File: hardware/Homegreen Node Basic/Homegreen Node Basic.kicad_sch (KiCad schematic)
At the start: 10 parts, among them J3 Conn_01x06_Pin, SW1 SW_Push, U1 ATtiny88-A

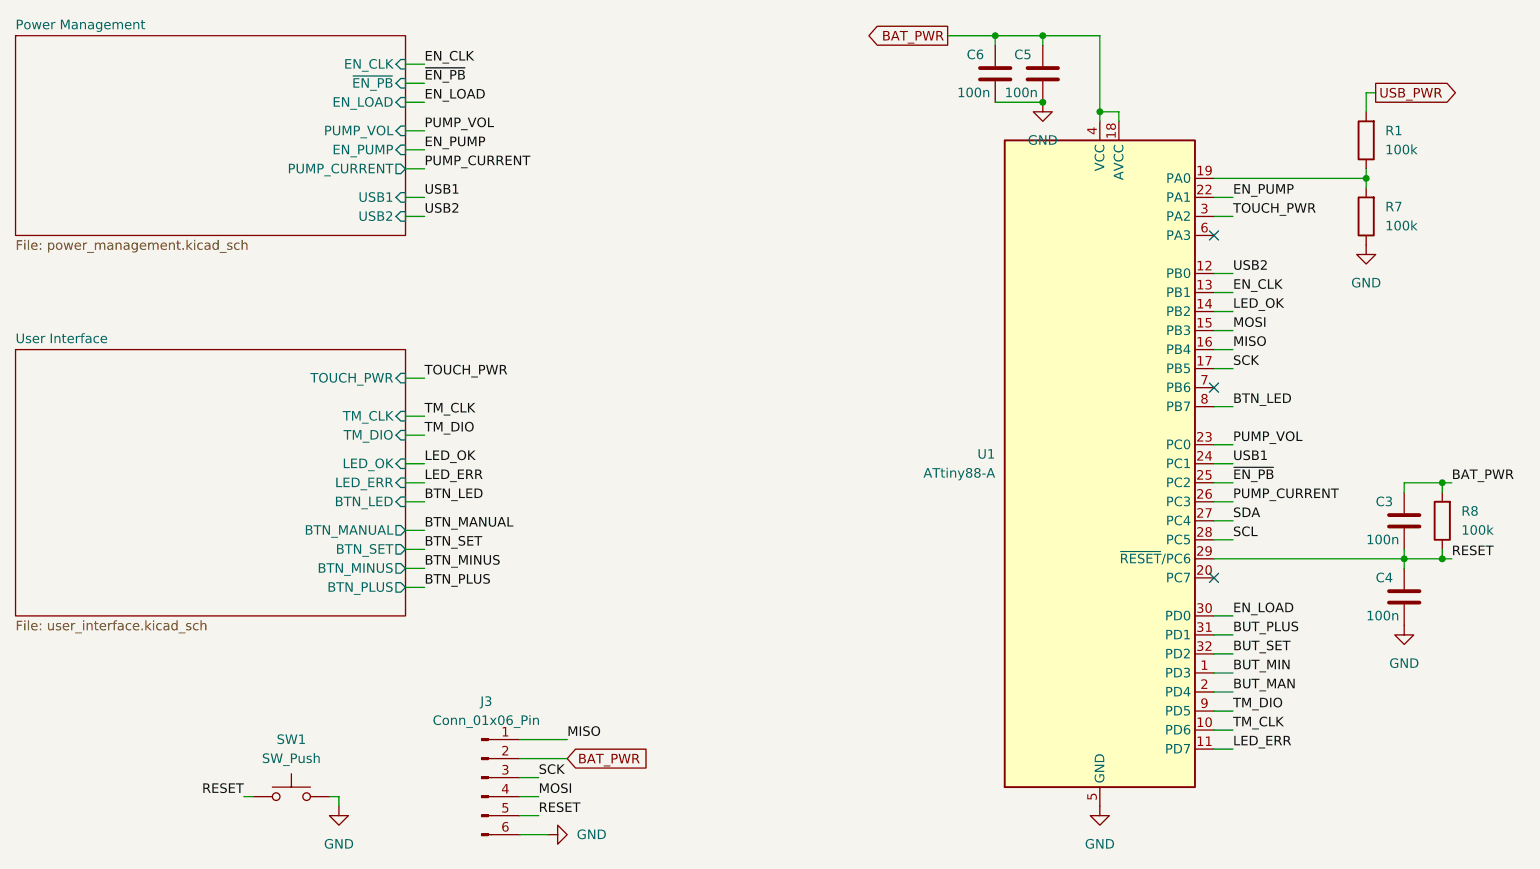
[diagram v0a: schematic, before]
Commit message: - starting with port to atmega328p
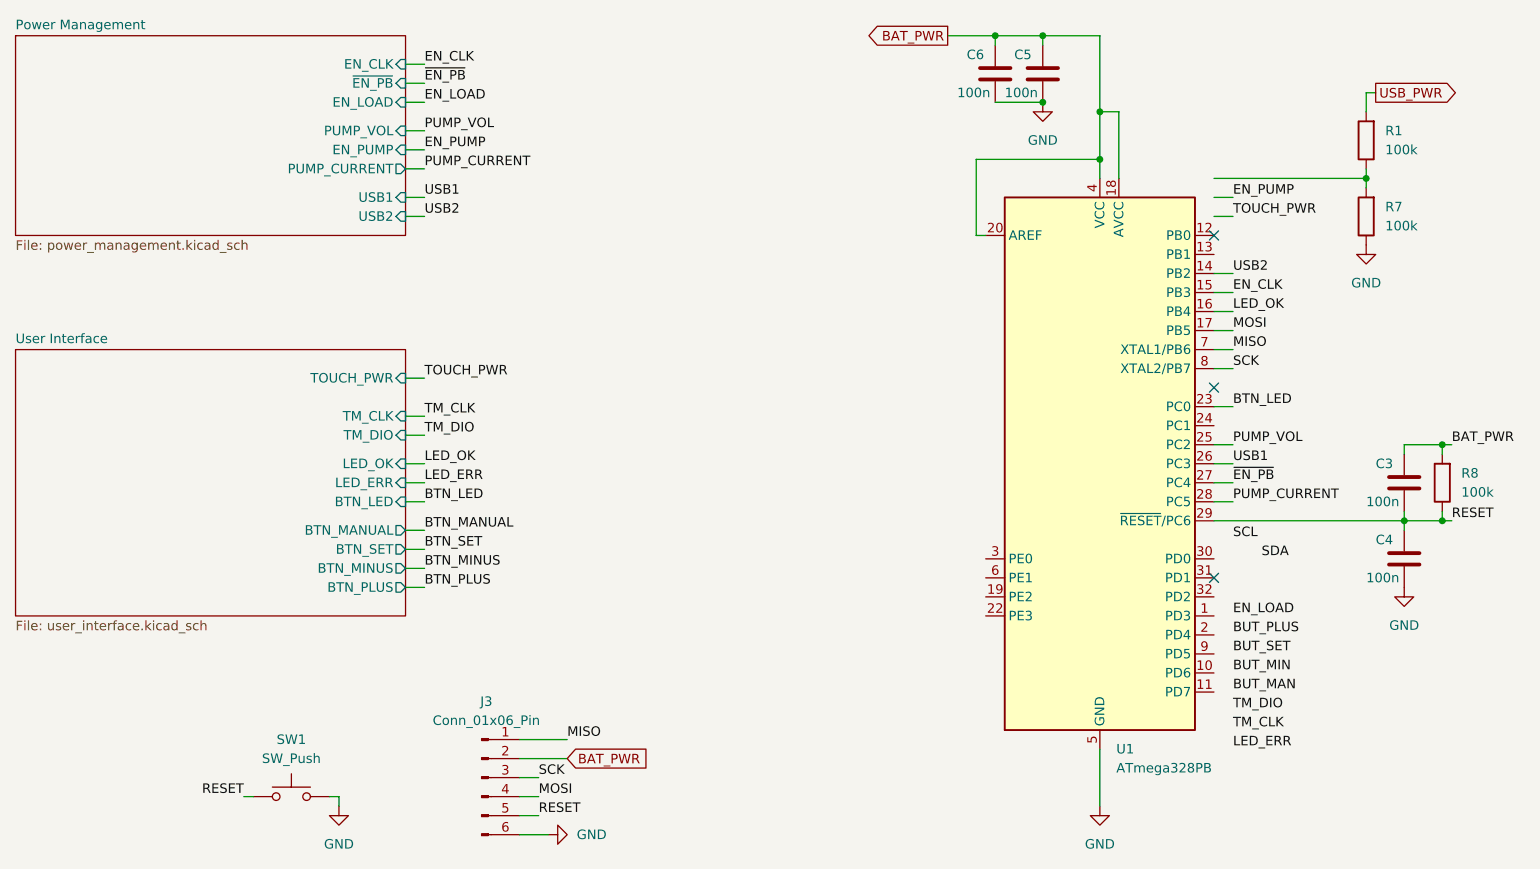
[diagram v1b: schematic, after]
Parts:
- U1: value ATtiny88-A -> ATmega328PB; symbol MCU_Microchip_ATtiny:ATtiny88-A -> MCU_Microchip_ATmega:ATmega328PB-A
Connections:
- net BAT_PWR: now also U1.20 (AREF)
- net BTN_LED: now also U1.23 (PC0); no longer U1.8 (PB7)
- net BUT_MAN: no longer U1.2 (PD4)
- net BUT_MIN: no longer U1.1 (PD3)
- net BUT_PLUS: no longer U1.31 (PD1)
- net BUT_SET: no longer U1.32 (PD2)
- net EN_CLK: now also U1.15 (PB3); no longer U1.13 (PB1)
- net EN_LOAD: no longer U1.30 (PD0)
- net EN_PUMP: no longer U1.22 (PA1)
- net LED_ERR: no longer U1.11 (PD7)
- net LED_OK: now also U1.16 (PB4); no longer U1.14 (PB2)
- net MISO: now also U1.7 (XTAL1/PB6); no longer U1.16 (PB4)
- net MOSI: now also U1.17 (PB5); no longer U1.15 (PB3)
- net PUMP_CURRENT: now also U1.28 (PC5); no longer U1.26 (PC3)
- net PUMP_VOL: now also U1.25 (PC2); no longer U1.23 (PC0)
- net SCK: now also U1.8 (XTAL2/PB7); no longer U1.17 (PB5)
- net SCL: no longer U1.28 (PC5)
- net SDA: no longer U1.27 (PC4)
- net TM_CLK: no longer U1.10 (PD6)
- net TM_DIO: no longer U1.9 (PD5)
- net TOUCH_PWR: no longer U1.3 (PA2)
- net USB1: now also U1.26 (PC3); no longer U1.24 (PC1)
- net USB2: now also U1.14 (PB2); no longer U1.12 (PB0)
- net ~{EN_PB}: now also U1.27 (PC4); no longer U1.25 (PC2)
- net at R1.1, R7.2: no longer U1.19 (PA0)
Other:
- moved on the sheet: C3, C4, R8, U1

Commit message: update PCB to 1-sided for price estimation
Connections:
- net PUMP_CURRENT: no longer names the net of U1.28 (PC5)
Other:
- sheet Power Management ports: added none; removed PUMP_CURRENT
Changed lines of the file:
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@@
-	(wire
-		(pts
-			(xy 90.17 52.07) (xy 92.71 52.07)
-		)
-		(stroke
-			(width 0)
-			(type default)
-		)
-	)
 	(wire
 		(pts
@@
 		(pts
 			(xy 90.17 91.44) (xy 92.71 91.44)
-		)
-		(stroke
-			(width 0)
-			(type default)
-		)
-	)
-	(wire
-		(pts
-			(xy 198.12 96.52) (xy 200.66 96.52)
 		)
 		(stroke
@@
 		)
 	)
-	(label "PUMP_CURRENT"
-		(at 200.66 96.52 0)
-		(fields_autoplaced yes)
-		(effects
-			(font
-				(size 1.27 1.27)
-			)
-			(justify left bottom)
-		)
-	)
 	(label "MOSI"
 		(at 107.95 135.89 0)
@@
 	(label "PUMP_VOL"
 		(at 200.66 88.9 0)
-		(fields_autoplaced yes)
-		(effects
-			(font
-				(size 1.27 1.27)
-			)
-			(justify left bottom)
-		)
-	)
-	(label "PUMP_CURRENT"
-		(at 92.71 52.07 0)
 		(fields_autoplaced yes)
 		(effects
@@
 			(effects
 				(font
-					(size 1.27 1.27)
-				)
-				(justify right)
-			)
-		)
-		(pin "PUMP_CURRENT" output
-			(at 90.17 52.07 0)
-			(effects
-				(font
